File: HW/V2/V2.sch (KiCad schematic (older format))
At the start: 0 parts

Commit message: V2 milling and BOM
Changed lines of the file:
@@
 F5 "SolderPWM1" I R 6350 3000 50
 F6 "MOSFETtemp" I R 6350 2700 50
-F7 "powerTemp" I R 6350 2300 50
-$EndSheet
-$Sheet
-S 7500 750  1950 1400
-U 5C556B0F
-F0 "Power" 50
-F1 "Power.sch" 50
-F2 "oneWireTemp" I L 7500 1950 50
 $EndSheet
 $Sheet
@@
 F2 "SolderPWM1" I L 7500 3000 50
 F3 "SolderPWM2" I L 7500 3100 50
-F4 "MOSFETtemp" I L 7500 2700 50
-F5 "oneWireTemp" I L 7500 2550 50
+F4 "oneWireTemp" I L 7500 2550 50
 $EndSheet
-Wire Wire Line
-	7500 2700 6350 2700
 $Sheet
 S 4500 4150 1900 1750
@@
 	7500 2550 7150 2550
 Wire Wire Line
-	6800 2550 6800 2300
+	6350 2700 7150 2700
 Wire Wire Line
-	6800 2300 6350 2300
-Wire Wire Line
-	7500 1950 7150 1950
-Wire Wire Line
-	7150 1950 7150 2550
-Connection ~ 7150 2550
-Wire Wire Line
-	7150 2550 6800 2550
+	7150 2700 7150 2550
+$Sheet
+S 7500 750  1950 1400
+U 5C556B0F
+F0 "Power" 50
+F1 "Power.sch" 50
+$EndSheet
 $EndSCHEMATC

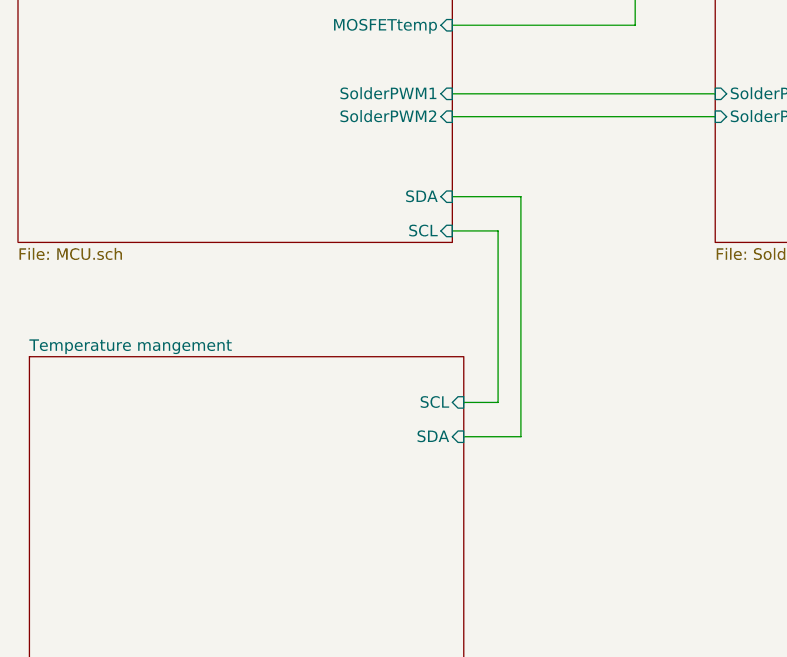
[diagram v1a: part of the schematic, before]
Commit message: piggyback ADC amp
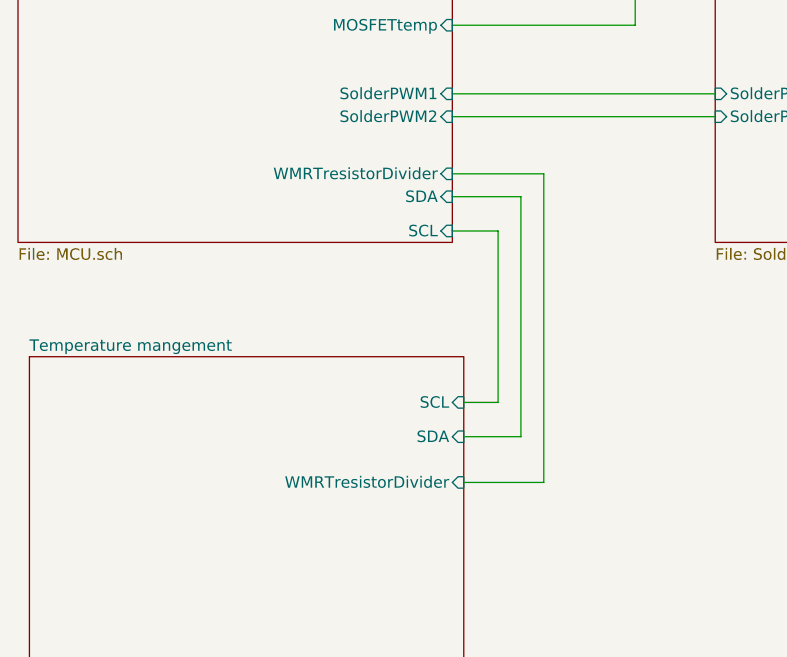
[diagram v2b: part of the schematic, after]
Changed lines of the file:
@@
 F5 "SolderPWM1" I R 6350 3000 50
 F6 "MOSFETtemp" I R 6350 2700 50
+F7 "WMRTresistorDivider" I R 6350 3350 50
 $EndSheet
 $Sheet
@@
 F2 "SDA" I R 6400 4500 50
 F3 "SCL" I R 6400 4350 50
+F4 "WMRTresistorDivider" I R 6400 4700 50
 $EndSheet
 Wire Wire Line
@@
 F1 "Power.sch" 50
 $EndSheet
+Wire Wire Line
+	6400 4700 6750 4700
+Wire Wire Line
+	6750 4700 6750 3350
+Wire Wire Line
+	6750 3350 6350 3350
 $EndSCHEMATC
